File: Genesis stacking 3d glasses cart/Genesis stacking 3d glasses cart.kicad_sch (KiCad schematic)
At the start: 29 parts, among them CON1 GENESIS-EDGE, J1 Conn_01x32_Male, J2 Conn_01x32_Male, J3 top slot connector, J4 3D Glasses, SW1 Pause, U1 74HC133, U2 74HC86, U3 74HC259, U4 LM324

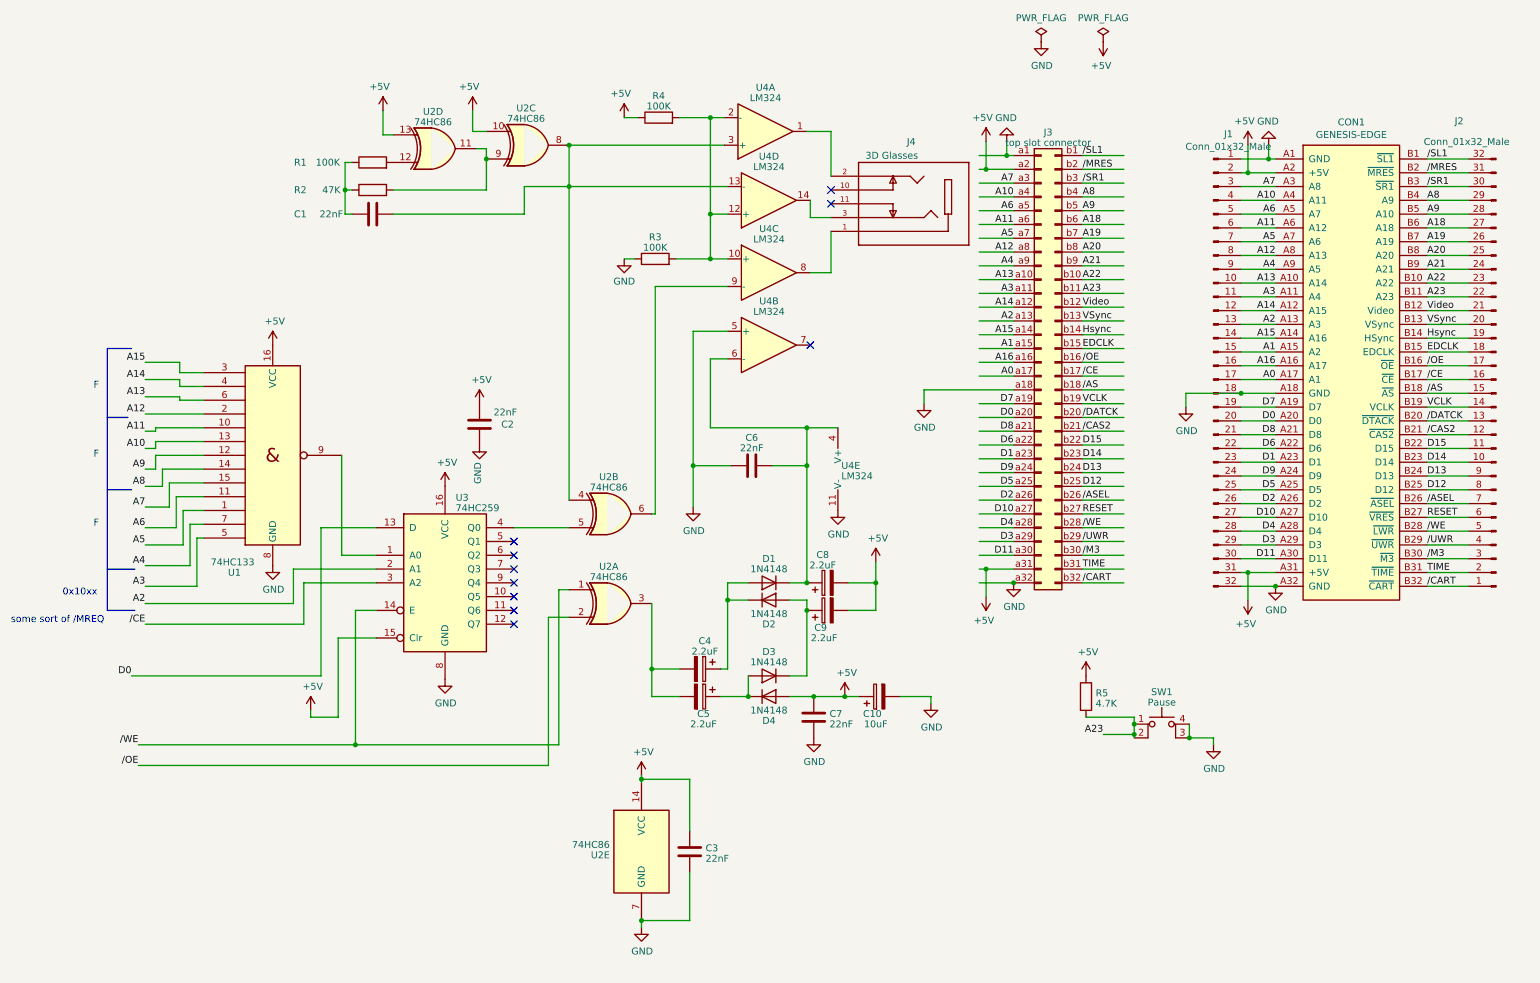
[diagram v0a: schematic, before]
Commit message: updated design, added reference materials
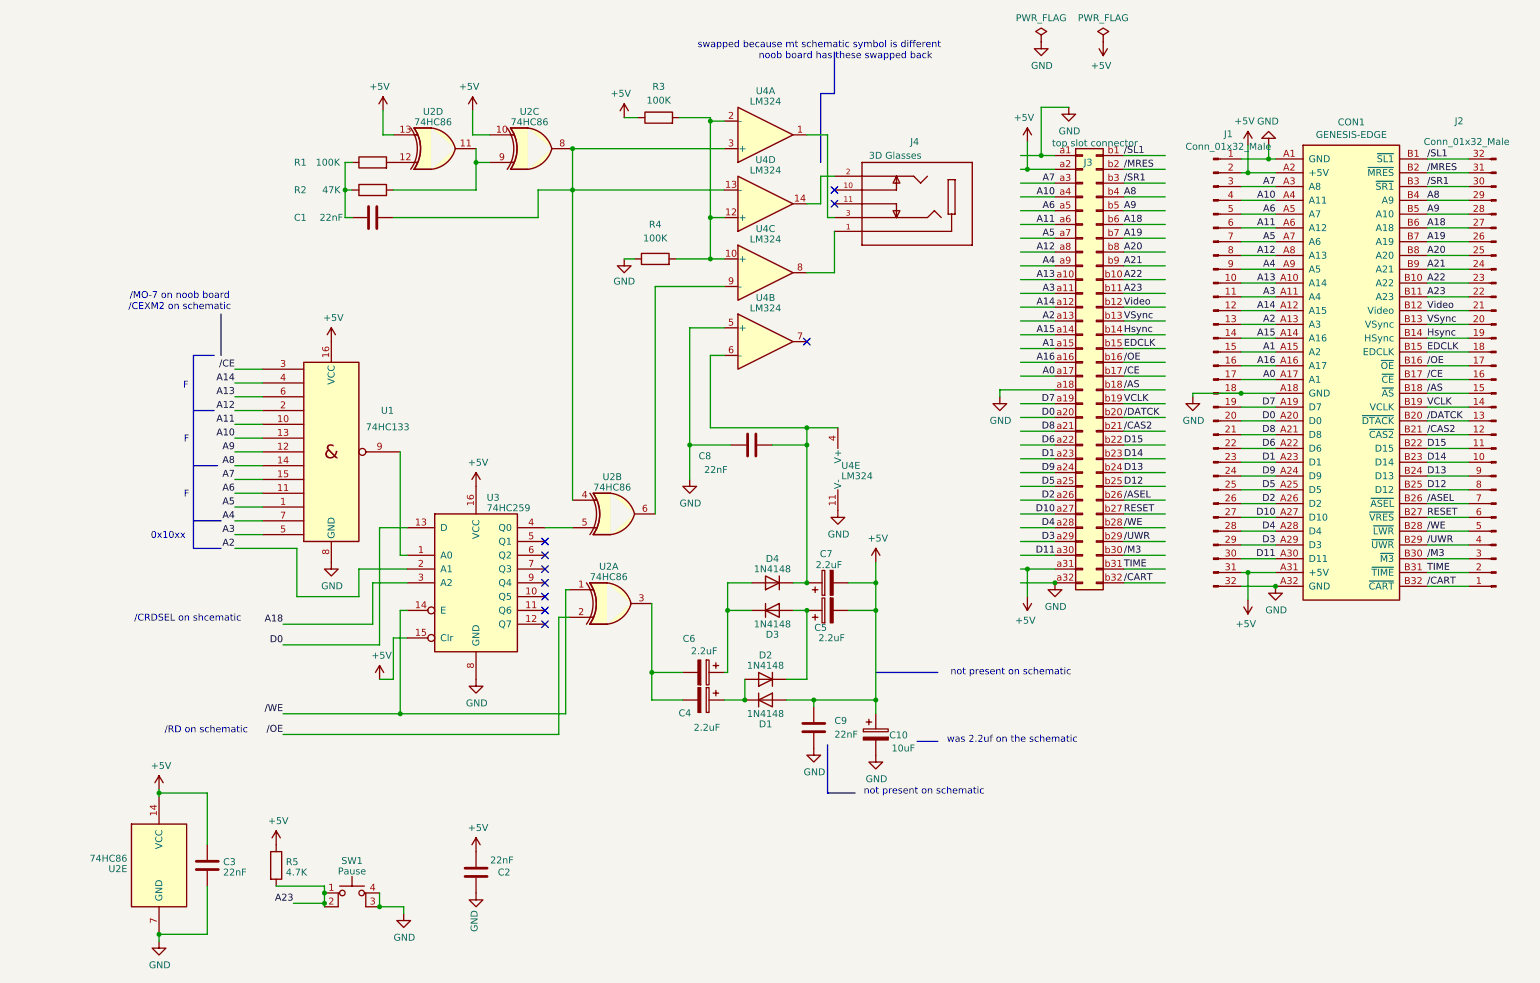
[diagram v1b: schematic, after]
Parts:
- renumbered C5 to C4, C9 to C5, C4 to C6, C8 to C7, C6 to C8, C7 to C9, D4 to D1, D3 to D2, D2 to D3, D1 to D4, R4 to R3, R3 to R4
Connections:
- net A15: no longer U1.3
- net A18: now also U3.3 (A2)
- net /CE: now also U1.3; no longer U3.3 (A2)
- net at J4.2: now also U4.14; no longer U4.1
- net at J4.3: now also U4.1; no longer U4.14
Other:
- note added: "/CRDSEL on shcematic"
- note added: "/MO-7 on noob board /CEXM2 on schematic"
- note added: "/RD on schematic"
- note added: "noob board has these swapped back"
- note added: "not present on schematic"
- note added: "swapped because mt schematic symbol is different"
- note added: "was 2.2uf on the schematic"
- note removed: "some sort of /MREQ"
- moved on the sheet: C1, C10, C2, C3, C4, C6, C8, C9, D1, D2, D3, D4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

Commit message: looks like last revision before fab
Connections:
- net at J4.2: now also U4.1; no longer U4.14
- net at J4.3: now also U4.14; no longer U4.1
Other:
- note removed: "noob board has these swapped back"
- note removed: "swapped because mt schematic symbol is different"
